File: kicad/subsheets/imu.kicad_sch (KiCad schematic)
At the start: 5 parts

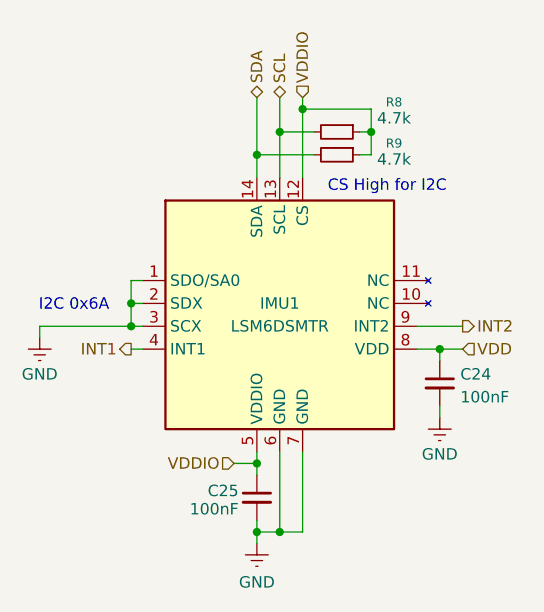
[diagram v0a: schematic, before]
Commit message: Footprint + silkscreen corrections
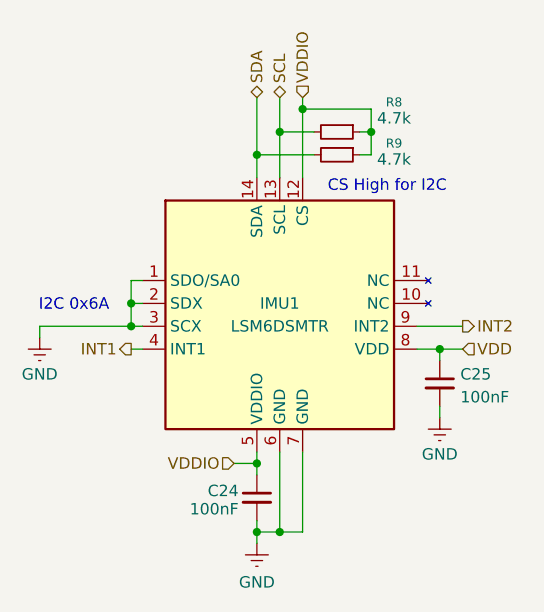
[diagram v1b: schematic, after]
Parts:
- C24: renamed from C25; now left out of the parts list
- C25: renamed from C24; now left out of the parts list
- IMU1, R8, R9: now left out of the parts list
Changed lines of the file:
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@@
 		(in_pos_files yes)
 		(dnp no)
-		(property "Reference" "#PWR027"
+		(property "Reference" "#PWR028"
 			(at 167.64 115.57 0)
 			(hide yes)
@@
 			(project "a3-srad-camera-v2"
 				(path "/c4ff1aa6-4aa7-4de3-a597-83271e910ec4/1e166fbb-82f8-45ac-ae24-8d2fc1672423"
-					(reference "#PWR027")
+					(reference "#PWR028")
 					(unit 1)
 				)
@@
 		(in_pos_files yes)
 		(dnp no)
-		(property "Reference" "#PWR028"
+		(property "Reference" "#PWR027"
 			(at 147.32 129.54 0)
 			(hide yes)
@@
 			(project "a3-srad-camera-v2"
 				(path "/c4ff1aa6-4aa7-4de3-a597-83271e910ec4/1e166fbb-82f8-45ac-ae24-8d2fc1672423"
-					(reference "#PWR028")
+					(reference "#PWR027")
 					(unit 1)
 				)
@@
 		(body_style 1)
 		(exclude_from_sim no)
-		(in_bom yes)
+		(in_bom no)
 		(on_board yes)
 		(in_pos_files yes)
@@
 		)
 		(property "SYMBOL" ""
+			(at 156.21 80.01 90)
+			(hide yes)
+			(show_name no)
+			(do_not_autoplace no)
+			(effects
+				(font
+					(size 1.27 1.27)
+				)
+			)
+		)
+		(property "KLC_S3.3" ""
+			(at 156.21 80.01 90)
+			(hide yes)
+			(show_name no)
+			(do_not_autoplace no)
+			(effects
+				(font
+					(size 1.27 1.27)
+				)
+			)
+		)
+		(property "KLC_S5.1" ""
 			(at 156.21 80.01 90)
 			(hide yes)
@@
 		(body_style 1)
 		(exclude_from_sim no)
-		(in_bom yes)
+		(in_bom no)
 		(on_board yes)
 		(in_pos_files yes)
@@
 		)
 		(property "SYMBOL" ""
+			(at 149.86 97.79 0)
+			(hide yes)
+			(show_name no)
+			(do_not_autoplace no)
+			(effects
+				(font
+					(size 1.27 1.27)
+				)
+			)
+		)
+		(property "KLC_S3.3" ""
+			(at 149.86 97.79 0)
+			(hide yes)
+			(show_name no)
+			(do_not_autoplace no)
+			(effects
+				(font
+					(size 1.27 1.27)
+				)
+			)
+		)
+		(property "KLC_S5.1" ""
 			(at 149.86 97.79 0)
 			(hide yes)
@@
 		(body_style 1)
 		(exclude_from_sim no)
-		(in_bom yes)
+		(in_bom no)
 		(on_board yes)
 		(in_pos_files yes)
 		(dnp no)
-		(property "Reference" "C24"
+		(property "Reference" "C25"
 			(at 169.926 104.394 0)
 			(show_name no)
@@
 		)
 		(property "SYMBOL" ""
+			(at 167.64 105.41 0)
+			(hide yes)
+			(show_name no)
+			(do_not_autoplace no)
+			(effects
+				(font
+					(size 1.27 1.27)
+				)
+			)
+		)
+		(property "KLC_S3.3" ""
+			(at 167.64 105.41 0)
+			(hide yes)
+			(show_name no)
+			(do_not_autoplace no)
+			(effects
+				(font
+					(size 1.27 1.27)
+				)
+			)
+		)
+		(property "KLC_S5.1" ""
 			(at 167.64 105.41 0)
 			(hide yes)
@@
 			(project "a3-srad-camera-v2"
 				(path "/c4ff1aa6-4aa7-4de3-a597-83271e910ec4/1e166fbb-82f8-45ac-ae24-8d2fc1672423"
-					(reference "C24")
+					(reference "C25")
 					(unit 1)
 				)
@@
 		(body_style 1)
 		(exclude_from_sim no)
-		(in_bom yes)
+		(in_bom no)
 		(on_board yes)
 		(in_pos_files yes)
 		(dnp no)
-		(property "Reference" "C25"
+		(property "Reference" "C24"
 			(at 145.288 117.348 0)
 			(show_name no)
@@
 		)
 		(property "SYMBOL" ""
+			(at 147.32 118.11 0)
+			(hide yes)
+			(show_name no)
+			(do_not_autoplace no)
+			(effects
+				(font
+					(size 1.27 1.27)
+				)
+			)
+		)
+		(property "KLC_S3.3" ""
+			(at 147.32 118.11 0)
+			(hide yes)
+			(show_name no)
+			(do_not_autoplace no)
+			(effects
+				(font
+					(size 1.27 1.27)
+				)
+			)
+		)
+		(property "KLC_S5.1" ""
 			(at 147.32 118.11 0)
 			(hide yes)
@@
 			(project "a3-srad-camera-v2"
 				(path "/c4ff1aa6-4aa7-4de3-a597-83271e910ec4/1e166fbb-82f8-45ac-ae24-8d2fc1672423"
-					(reference "C25")
+					(reference "C24")
 					(unit 1)
 				)
@@
 		(body_style 1)
 		(exclude_from_sim no)
-		(in_bom yes)
+		(in_bom no)
 		(on_board yes)
 		(in_pos_files yes)
@@
 			(at 156.21 77.47 90)
 			(hide yes)
+			(show_name no)
+			(do_not_autoplace no)
+			(effects
+				(font
+					(size 1.27 1.27)
+				)
+			)
+		)
+		(property "KLC_S3.3" ""
+			(at 156.21 77.47 90)
+			(hide yes)
+			(show_name no)
+			(do_not_autoplace no)
+			(effects
+				(font
+					(size 1.27 1.27)
+				)
+			)
+		)
+		(property "KLC_S5.1" ""
+			(at 156.21 77.47 90)
+			(hide yes)

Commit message: Minor kicad changes
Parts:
- C24, C25, IMU1, R8, R9: BOARD_SIDE (none) -> Front; now in the parts list
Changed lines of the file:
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@@
 		(body_style 1)
 		(exclude_from_sim no)
-		(in_bom no)
+		(in_bom yes)
 		(on_board yes)
 		(in_pos_files yes)
@@
 		)
 		(property "KLC_S5.1" ""
+			(at 156.21 80.01 90)
+			(hide yes)
+			(show_name no)
+			(do_not_autoplace no)
+			(effects
+				(font
+					(size 1.27 1.27)
+				)
+			)
+		)
+		(property "BOARD_SIDE" "Front"
 			(at 156.21 80.01 90)
 			(hide yes)
@@
 		(body_style 1)
 		(exclude_from_sim no)
-		(in_bom no)
+		(in_bom yes)
 		(on_board yes)
 		(in_pos_files yes)
@@
 		)
 		(property "KLC_S5.1" ""
+			(at 149.86 97.79 0)
+			(hide yes)
+			(show_name no)
+			(do_not_autoplace no)
+			(effects
+				(font
+					(size 1.27 1.27)
+				)
+			)
+		)
+		(property "BOARD_SIDE" "Front"
 			(at 149.86 97.79 0)
 			(hide yes)
@@
 		(body_style 1)
 		(exclude_from_sim no)
-		(in_bom no)
+		(in_bom yes)
 		(on_board yes)
 		(in_pos_files yes)
@@
 		)
 		(property "KLC_S5.1" ""
+			(at 167.64 105.41 0)
+			(hide yes)
+			(show_name no)
+			(do_not_autoplace no)
+			(effects
+				(font
+					(size 1.27 1.27)
+				)
+			)
+		)
+		(property "BOARD_SIDE" "Front"
 			(at 167.64 105.41 0)
 			(hide yes)
@@
 		(body_style 1)
 		(exclude_from_sim no)
-		(in_bom no)
+		(in_bom yes)
 		(on_board yes)
 		(in_pos_files yes)
@@
 		)
 		(property "KLC_S5.1" ""
+			(at 147.32 118.11 0)
+			(hide yes)
+			(show_name no)
+			(do_not_autoplace no)
+			(effects
+				(font
+					(size 1.27 1.27)
+				)
+			)
+		)
+		(property "BOARD_SIDE" "Front"
 			(at 147.32 118.11 0)
 			(hide yes)
@@
 		(body_style 1)
 		(exclude_from_sim no)
-		(in_bom no)
+		(in_bom yes)
 		(on_board yes)
 		(in_pos_files yes)
@@
 			(at 156.21 77.47 90)
 			(hide yes)
+			(show_name no)
+			(do_not_autoplace no)
+			(effects
+				(font
+					(size 1.27 1.27)
+				)
+			)
+		)
+		(property "BOARD_SIDE" "Front"
+			(at 156.21 77.47 90)
+			(hide yes)
